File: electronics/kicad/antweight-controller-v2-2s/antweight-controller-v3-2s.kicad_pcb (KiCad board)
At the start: 2 copper layers, 100 x 100 mm, 23 parts, among them J10 3V3 GND VBAT_SW, J4 FUSED 2S INPUT, J5 MOTOR LEFT, J6 MOTOR RIGHT, J8 ESP32 LEFT ALL PINS, J9 ESP32 RIGHT SIGNALS, SW1 MAIN POWER, U1 ESP32-C3 SUPERMINI, U2 DRV8833, U3 MINI-360 MP2307DN 3V3

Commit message: chore: checkpoint v2/v3 2S PCB routing refactor progress
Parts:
- moved U2 14.2 mm to (100.3, 95.0), turned to 180 degrees
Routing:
- net M2B: track 36.3 -> 30.3 mm
- net M1B: track 39.1 -> 33.1 mm
- net VBAT_SW: track 101.0 -> 98.0 mm
- net 3V3: track 86.6 -> 83.6 mm
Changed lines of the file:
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@@
 	(footprint "DRV8833_MACHINED_SOCKET_VERIFY"
 		(layer "F.Cu")
-		(at 99.2 80.875 -90)
+		(at 100.32 94.995 180)
 		(property "Reference" "U2"
-			(at 0 -3 0)
+			(at 0 -3 90)
 			(layer "F.Fab")
 			(hide yes)
@@
 		)
 		(property "Value" "DRV8833"
-			(at 7.62 16 0)
+			(at 7.62 16 90)
 			(layer "F.Fab")
 			(hide yes)
@@
 		)
 		(property "Datasheet" ""
-			(at 0 0 0)
+			(at 0 0 90)
 			(layer "F.Fab")
 			(hide yes)
@@
 		)
 		(property "Description" ""
-			(at 0 0 0)
+			(at 0 0 90)
 			(layer "F.Fab")
 			(hide yes)
@@
 		)
 		(pad "1" thru_hole rect
-			(at 0 0)
+			(at 0 0 270)
 			(size 2 2)
 			(drill 1)
@@
 		)
 		(pad "2" thru_hole circle
-			(at 15.24 0)
+			(at 15.24 0 270)
 			(size 2 2)
 			(drill 1)
@@
 		)
 		(pad "3" thru_hole circle
-			(at 0 2.54)
+			(at 0 2.54 270)
 			(size 2 2)
 			(drill 1)
@@
 		)
 		(pad "4" thru_hole circle
-			(at 15.24 2.54)
+			(at 15.24 2.54 270)
 			(size 2 2)
 			(drill 1)
@@
 		)
 		(pad "5" thru_hole circle
-			(at 0 5.08)
+			(at 0 5.08 270)
 			(size 2 2)
 			(drill 1)
@@
 		)
 		(pad "6" thru_hole circle
-			(at 15.24 5.08)
+			(at 15.24 5.08 270)
 			(size 2 2)
 			(drill 1)
@@
 		)
 		(pad "7" thru_hole circle
-			(at 0 7.62)
+			(at 0 7.62 270)
 			(size 2 2)
 			(drill 1)
@@
 		)
 		(pad "8" thru_hole circle
-			(at 15.24 7.62)
+			(at 15.24 7.62 270)
 			(size 2 2)
 			(drill 1)
@@
 		)
 		(pad "9" thru_hole circle
-			(at 0 10.16)
+			(at 0 10.16 270)
 			(size 2 2)
 			(drill 1)
@@
 		)
 		(pad "10" thru_hole circle
-			(at 15.24 10.16)
+			(at 15.24 10.16 270)
 			(size 2 2)
 			(drill 1)
@@
 		)
 		(pad "11" thru_hole circle
-			(at 0 12.7)
+			(at 0 12.7 270)
 			(size 2 2)
 			(drill 1)
@@
 		)
 		(pad "12" thru_hole circle
-			(at 15.24 12.7)
+			(at 15.24 12.7 270)
 			(size 2 2)
 			(drill 1)
@@
 		)
 	)
-	(gr_text "MOTOR DRIVER"
-		(at 92.8 88.2 0)
+	(gr_text "FLT"
+		(at 87.82 82.175 0)
+		(layer "F.SilkS")
+		(effects
+			(font
+				(size 0.8 0.8)
+				(thickness 0.12)
+			)
+		)
+	)
+	(gr_text "M2B"
+		(at 87.82 84.715 0)
+		(layer "F.SilkS")
+		(effects
+			(font
+				(size 0.8 0.8)
+				(thickness 0.12)
+			)
+		)
+	)
+	(gr_text "M2A"
+		(at 87.82 87.255 0)
+		(layer "F.SilkS")
+		(effects
+			(font
+				(size 0.8 0.8)
+				(thickness 0.12)
+			)
+		)
+	)
+	(gr_text "M1B"
+		(at 87.82 89.795 0)
+		(layer "F.SilkS")
+		(effects
+			(font
+				(size 0.8 0.8)
+				(thickness 0.12)
+			)
+		)
+	)
+	(gr_text "M1A"
+		(at 87.82 92.335 0)
 		(layer "F.SilkS")
 		(effects
@@
 		)
 	)
+	(gr_text "VCC"
+		(at 97.32 87.675 0)
+		(layer "F.SilkS")
+		(effects
+			(font
+				(size 0.8 0.8)
+				(thickness 0.12)
+			)
+		)
+	)
+	(gr_text "GND"
+		(at 97.32 90.215 0)
+		(layer "F.SilkS")
+		(effects
+			(font
+				(size 0.8 0.8)
+				(thickness 0.12)
+			)
+		)
+	)
+	(gr_text "AI1"
+		(at 97.52 82.595 0)
+		(layer "F.SilkS")
+		(effects
+			(font
+				(size 0.8 0.8)
+				(thickness 0.12)
+			)
+		)
+	)
+	(gr_text "AI2"
+		(at 97.52 85.135 0)
+		(layer "F.SilkS")
+		(effects
+			(font
+				(size 0.8 0.8)
+				(thickness 0.12)
+			)
+		)
+	)
+	(gr_text "BI1"
+		(at 97.52 92.755 0)
+		(layer "F.SilkS")
+		(effects
+			(font
+				(size 0.8 0.8)
+				(thickness 0.12)
+			)
+		)
+	)
+	(gr_text "BI2"
+		(at 97.52 95.295 0)
+		(layer "F.SilkS")
+		(effects
+			(font
+				(size 0.8 0.8)
+				(thickness 0.12)
+			)
+		)
+	)
 	(gr_text "HDR R"
 		(at 104.7 79.2 0)
@@
 		)
 	)
-	(gr_text "FLT"
-		(at 86.38 93.375 90)
-		(layer "F.SilkS")
-		(effects
-			(font
-				(size 0.8 0.8)
-				(thickness 0.12)
-			)
-		)
-	)
-	(gr_text "AI1"
-		(at 86.8 83.675 90)
-		(layer "F.SilkS")
-		(effects
-			(font
-				(size 0.8 0.8)
-				(thickness 0.12)
-			)
-		)
-	)
-	(gr_text "M2B"
-		(at 88.92 93.375 90)
-		(layer "F.SilkS")
-		(effects
-			(font
-				(size 0.8 0.8)
-				(thickness 0.12)
-			)
-		)
-	)
-	(gr_text "AI2"
-		(at 89.34 83.675 90)
-		(layer "F.SilkS")
-		(effects
-			(font
-				(size 0.8 0.8)
-				(thickness 0.12)
-			)
-		)
-	)
-	(gr_text "M2A"
-		(at 91.46 93.375 90)
-		(layer "F.SilkS")
-		(effects
-			(font
-				(size 0.8 0.8)
-				(thickness 0.12)
-			)
-		)
-	)
-	(gr_text "VCC"
-		(at 91.88 83.875 90)
-		(layer "F.SilkS")
-		(effects
-			(font
-				(size 0.8 0.8)
-				(thickness 0.12)
-			)
-		)
-	)
-	(gr_text "M1B"
-		(at 94 93.375 90)
-		(layer "F.SilkS")
-		(effects
-			(font
-				(size 0.8 0.8)
-				(thickness 0.12)
-			)
-		)
-	)
-	(gr_text "GND"
-		(at 94.42 83.875 90)
-		(layer "F.SilkS")
-		(effects
-			(font
-				(size 0.8 0.8)
-				(thickness 0.12)
-			)
-		)
-	)
-	(gr_text "M1A"
-		(at 96.54 93.375 90)
-		(layer "F.SilkS")
-		(effects
-			(font
-				(size 0.8 0.8)
-				(thickness 0.12)
-			)
-		)
-	)
-	(gr_text "BI1"
-		(at 96.96 83.675 90)
-		(layer "F.SilkS")
-		(effects
-			(font
-				(size 0.8 0.8)
-				(thickness 0.12)
-			)
-		)
-	)
 	(gr_text "B+"
-		(at 94.0 104.0 90)
-		(layer "F.SilkS")
-		(effects
-			(font
-				(size 0.8 0.8)
-				(thickness 0.12)
-			)
-		)
-	)
-	(gr_text "BI2"
-		(at 99.5 83.675 90)
+		(at 98.2 111.2 90)
 		(layer "F.SilkS")
 		(effects
@@
 	(gr_text "M1B"
 		(at 105.5 93.315 90)
+		(layer "F.SilkS")
+		(effects
+			(font
+				(size 0.8 0.8)
+				(thickness 0.12)
+			)
+		)
+	)
+	(gr_text "MOTOR DRIVER"
+		(at 92.995 88.595 270)
 		(layer "F.SilkS")
 		(effects
@@
 	)
 	(segment
-		(start 99.2 96.115)
-		(end 100.04 91.375)
+		(start 85.08 94.995)
+		(end 89.82 95.835)
 		(width 0.8)
 		(layer "B.Cu")
@@
 	)
 	(segment
-		(start 91.58 80.875)
-		(end 91.58 78.85)
+		(start 100.32 87.375)
+		(end 102.345 87.375)
 		(width 1.5)
 		(layer "F.Cu")
@@
 	(segment
 		(start 110 78.85)
-		(end 110 104.25)
+		(end 110 101.25)
 		(width 1.5)
 		(layer "B.Cu")
@@
 	)
 	(segment
-		(start 77.15 113.125)
+		(start 77.15 110.125)
 		(end 77.15 64.255)
 		(width 0.8)
@@
 	)
 	(segment
-		(start 89.04 83)
-		(end 89.04 80.875)
+		(start 98.195 84.835)
+		(end 100.32 84.835)
 		(width 0.25)
 		(layer "B.Cu")
@@
 	)
 	(segment
-		(start 86.5 83.6)
-		(end 86.5 80.875)
+		(start 97.595 82.295)
+		(end 100.32 82.295)
 		(width 0.25)
 		(layer "F.Cu")
@@
 	)
 	(segment
-		(start 96.66 83)
-		(end 96.66 80.875)
+		(start 98.195 92.455)
+		(end 100.32 92.455)
 		(width 0.25)
 		(layer "F.Cu")
@@
 	)
 	(segment
-		(start 99.2 84.5)
-		(end 99.2 80.875)
+		(start 96.695 94.995)
+		(end 100.32 94.995)
 		(width 0.25)
 		(layer "B.Cu")
@@
 	)
 	(segment
-		(start 96.66 96.115)
-		(end 96.66 98.5)
+		(start 85.08 92.455)
+		(end 82.695 92.455)
 		(width 1)
 		(layer "B.Cu")
@@
 	(segment
 		(start 94.12 96.115)
-		(end 94.12 102)
+		(end 94.12 99)
 		(width 1)
 		(layer "F.Cu")
@@
 	)
 	(segment
-		(start 106 102)
+		(start 106 99)
 		(end 106 84.5)
 		(width 1)
@@
 	)
 	(segment
-		(start 91.58 96.115)
-		(end 91.58 98.5)
+		(start 85.08 87.375)
+		(end 82.695 87.375)
 		(width 1)
 		(layer "B.Cu")
@@
 	)
 	(segment
-		(start 80 102)
+		(start 80 99)
 		(end 80 84.5)
 		(width 1)
@@
 	(segment
 		(start 89.04 96.115)
-		(end 89.04 102)
+		(end 89.04 99)
 		(width 1)
 		(layer "F.Cu")

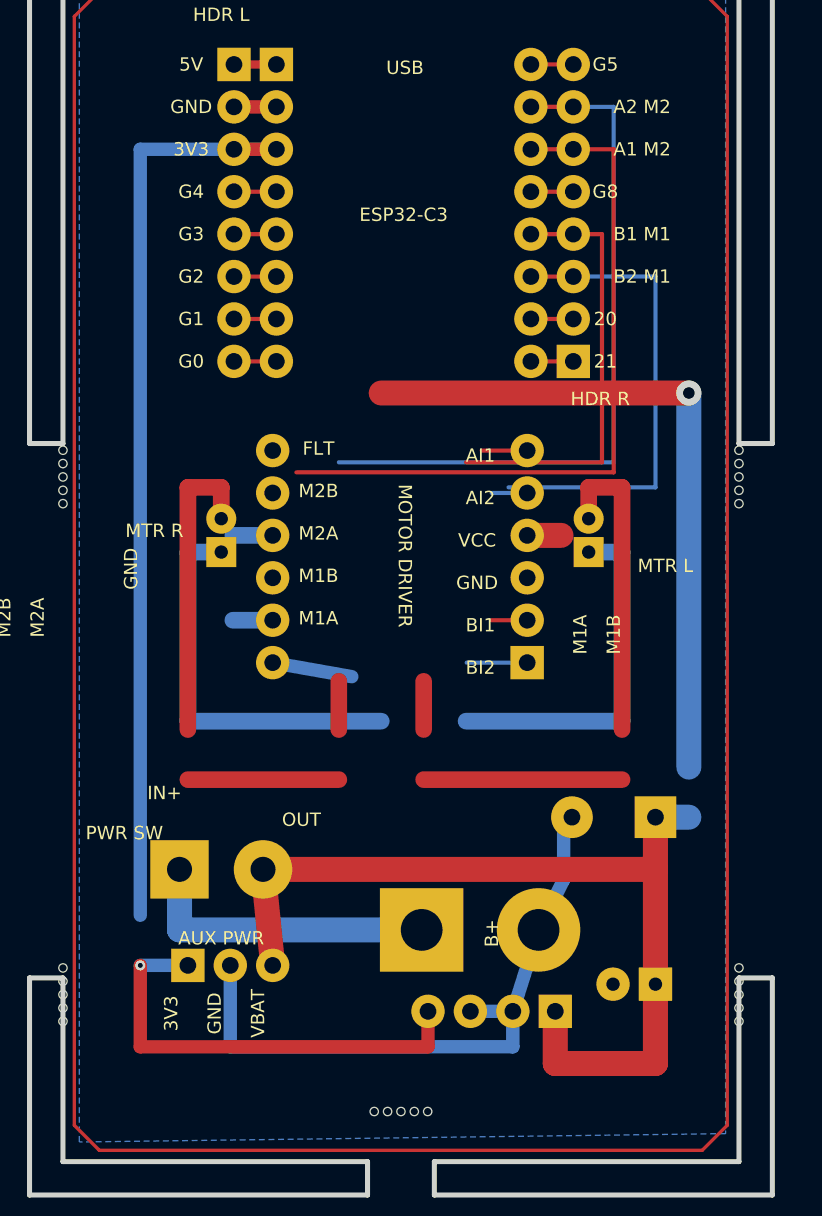
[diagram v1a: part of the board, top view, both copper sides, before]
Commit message: chore(electronics): refine v2/v3 2S PCB routing and DRC fixes
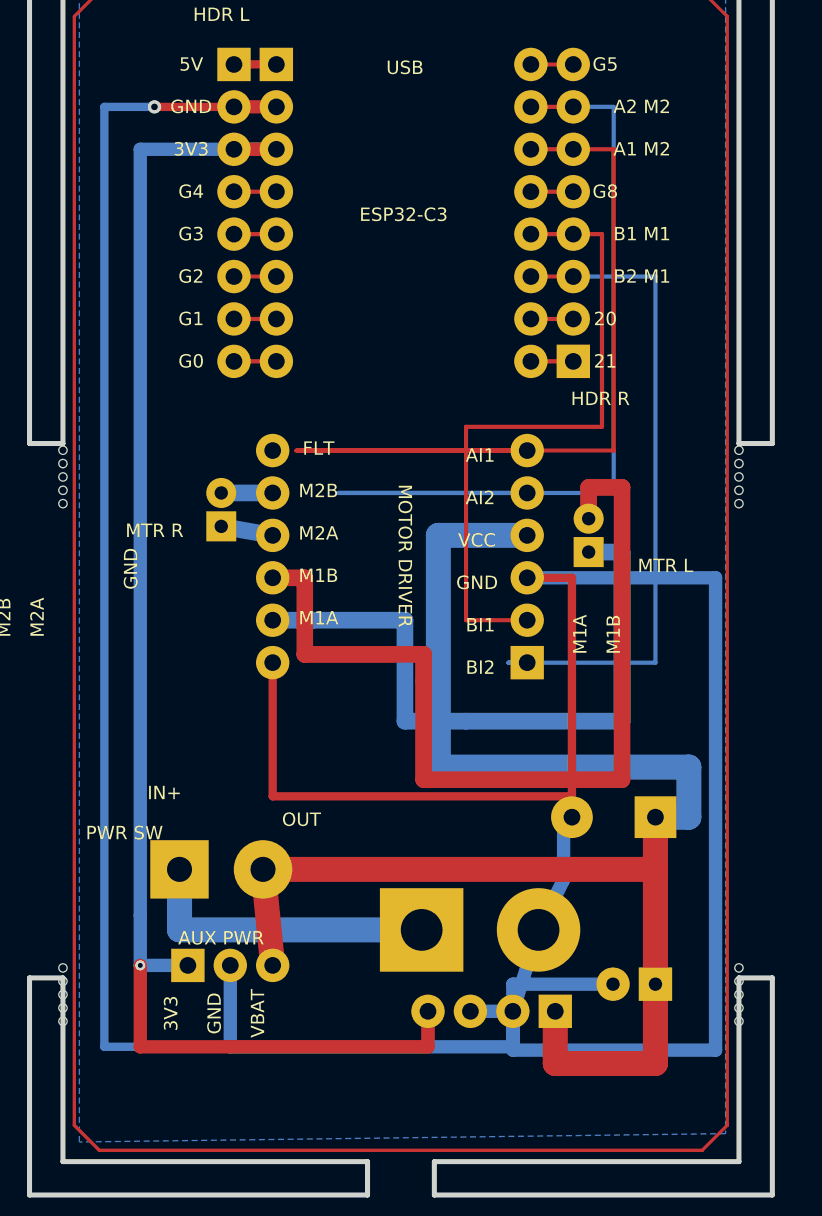
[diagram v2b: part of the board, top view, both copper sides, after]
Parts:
- removed MB2: MOUSE_BITE, MOUSE_BITE_5X0.5
- moved J6 1.54 mm to (82.0, 86.8)
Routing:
- net GND: track 45.9 -> 218.6 mm, vias 0 -> 1
- net M2B: track 30.3 -> 3.08 mm
- net M2A: track 26.1 -> 3.13 mm
- net M1B: track 33.1 -> 54.4 mm
- net M1A: track 23.9 -> 39.1 mm
- net BIN1_GPIO9: track 28.2 -> 39.2 mm
- net AIN2_GPIO6: track 44.8 -> 55.8 mm
- net AIN1_GPIO7: track 46.0 -> 55.8 mm
- net BIN2_GPIO10: track 32.5 -> 40.5 mm
- net VBAT_SW: track 98.0 -> 92.3 mm, vias 1 -> 0
- net 3V3: track 83.6 -> 86.6 mm
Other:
- board text removed: "B+"

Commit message: Update docs and publish KiCad WIP state
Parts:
- moved J5 7.14 mm to (110.0, 84.5)
- moved U3 6.14 mm to (98.6, 121.0)
- moved J6 3.80 mm to (79.0, 84.5)
- moved J10 1.88 mm to (79.9, 115.0)
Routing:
- net M1B: track 54.4 -> 77.3 mm
- net GND: track 218.6 -> 238.8 mm
- net M1A: track 39.1 -> 45.0 mm
- net M2A: track 3.13 -> 6.73 mm
- net M2B: track 3.08 -> 6.51 mm
- net 3V3: track 86.6 -> 89.5 mm
- net VBAT_SW: track 92.3 -> 94.7 mm
